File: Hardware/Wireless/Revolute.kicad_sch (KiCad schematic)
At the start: 56 parts, among them Q1 NMOS, U11 LSM6DSO, U2 Button, U2 nrf52833_qfn40, U3 AS5600, U4 MIC5504, U5 BQ24075RGT, U7 Conn_01x14_Socket, X1 32.768 kHz, X2 32MHZ

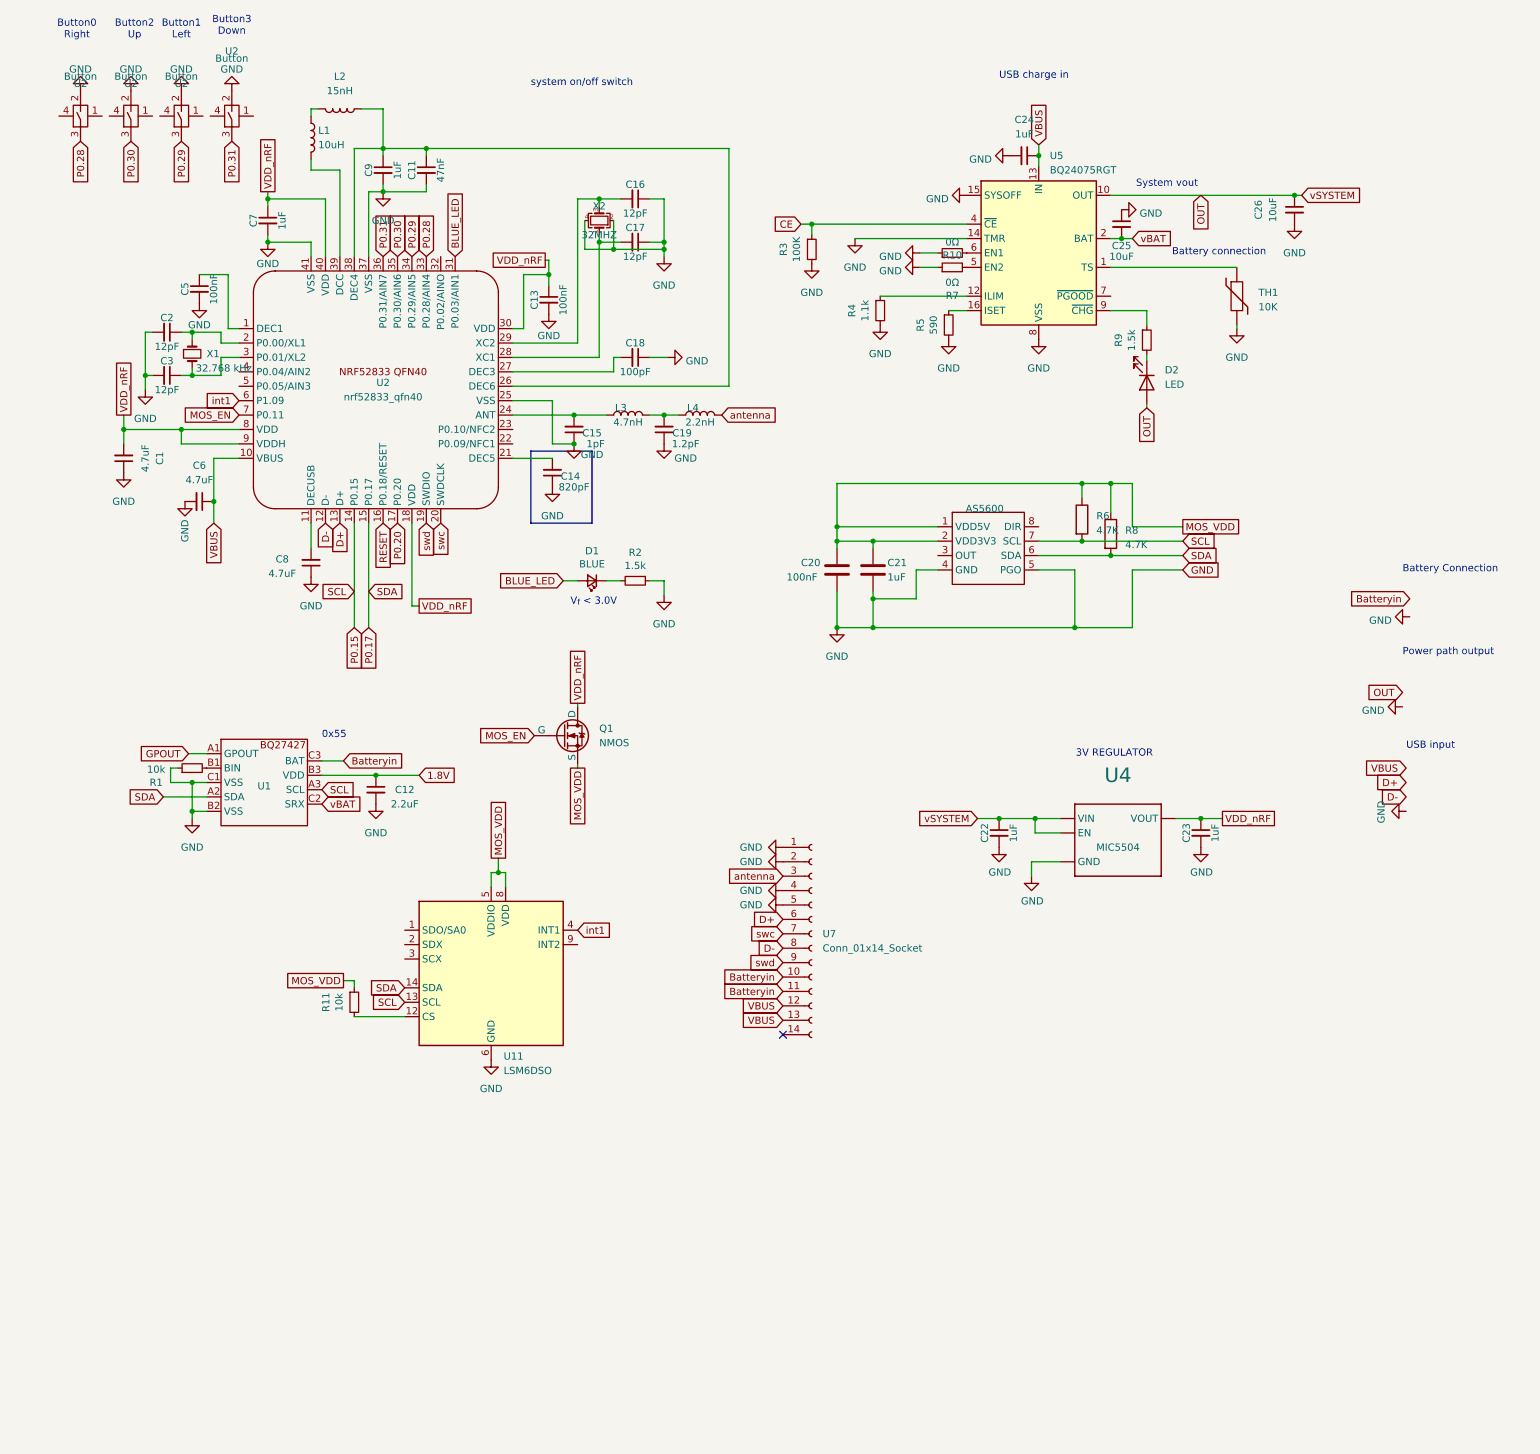
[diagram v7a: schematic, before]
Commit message: changed board shape, adedd unrouted test board, added active rectifier for reverse polarity, changed fuel gauge ic to smaller
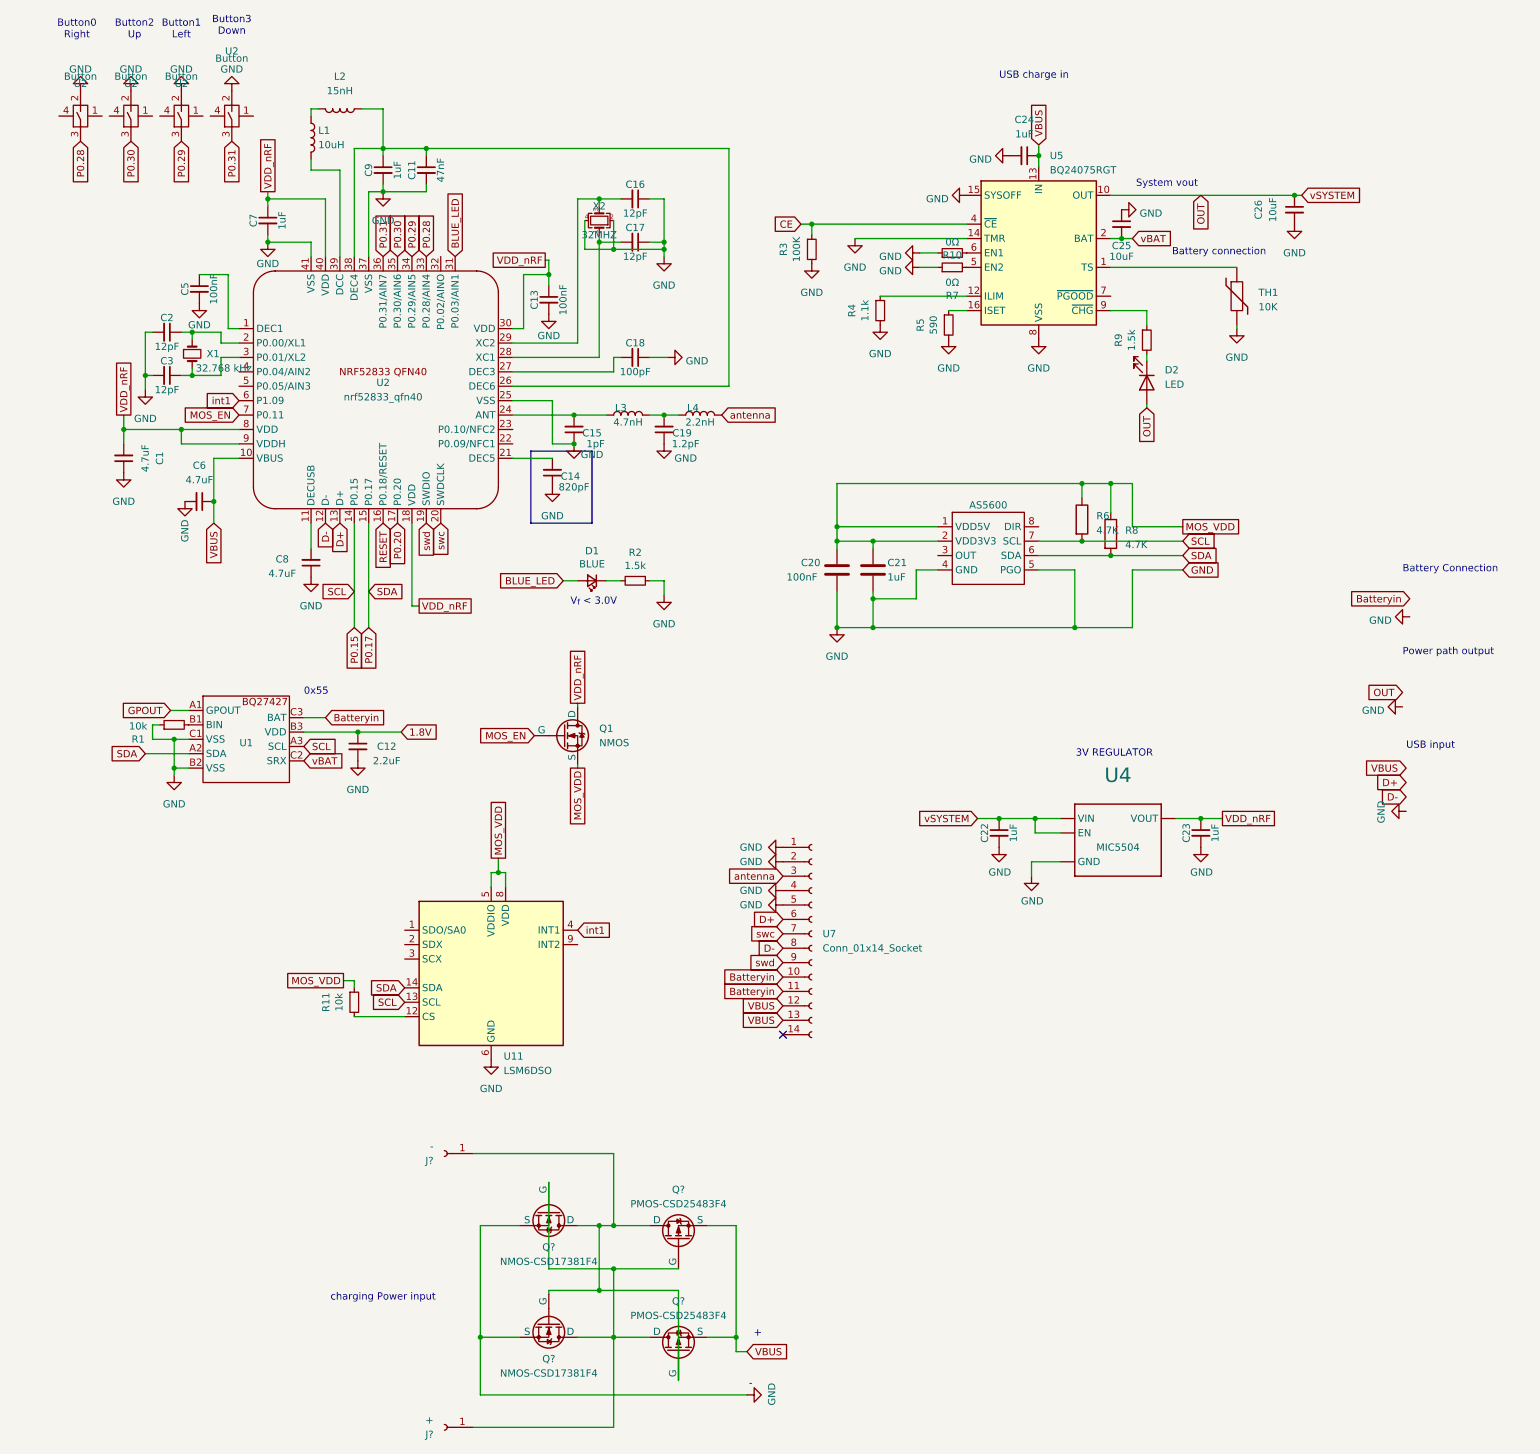
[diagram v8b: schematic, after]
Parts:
- added J?: -, Library:Pogo-pin-recepticle, symbol Connector:Conn_01x01_Socket
- added J?: +, Library:Pogo-pin-recepticle, symbol Connector:Conn_01x01_Socket
- added Q? (x2): PMOS-CSD25483F4, Library:Mosfet0402, symbol Simulation_SPICE:PMOS
- added Q? (x2): NMOS-CSD17381F4, Library:Mosfet0402, symbol Simulation_SPICE:NMOS
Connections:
- net GND: now also Q?.2 (S), Q?.2 (S)
- net VBUS: now also Q?.2 (S), Q?.2 (S)
- new net: J?.1 (Pin_1), Q?.1 (G), Q?.1 (G), Q?.3 (D), Q?.3 (D) (x2)
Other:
- note added: "+"
- note added: "-"
- note added: "charging Power input"
- note removed: "system on/off switch"
- moved on the sheet: C12, R1, U1
